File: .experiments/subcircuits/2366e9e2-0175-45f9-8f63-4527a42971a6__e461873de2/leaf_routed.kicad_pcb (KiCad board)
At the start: 2 copper layers, 49.9 x 20.9 mm, 7 parts, among them J2 Output, J3 Debug, U5 AP2112K-3.3

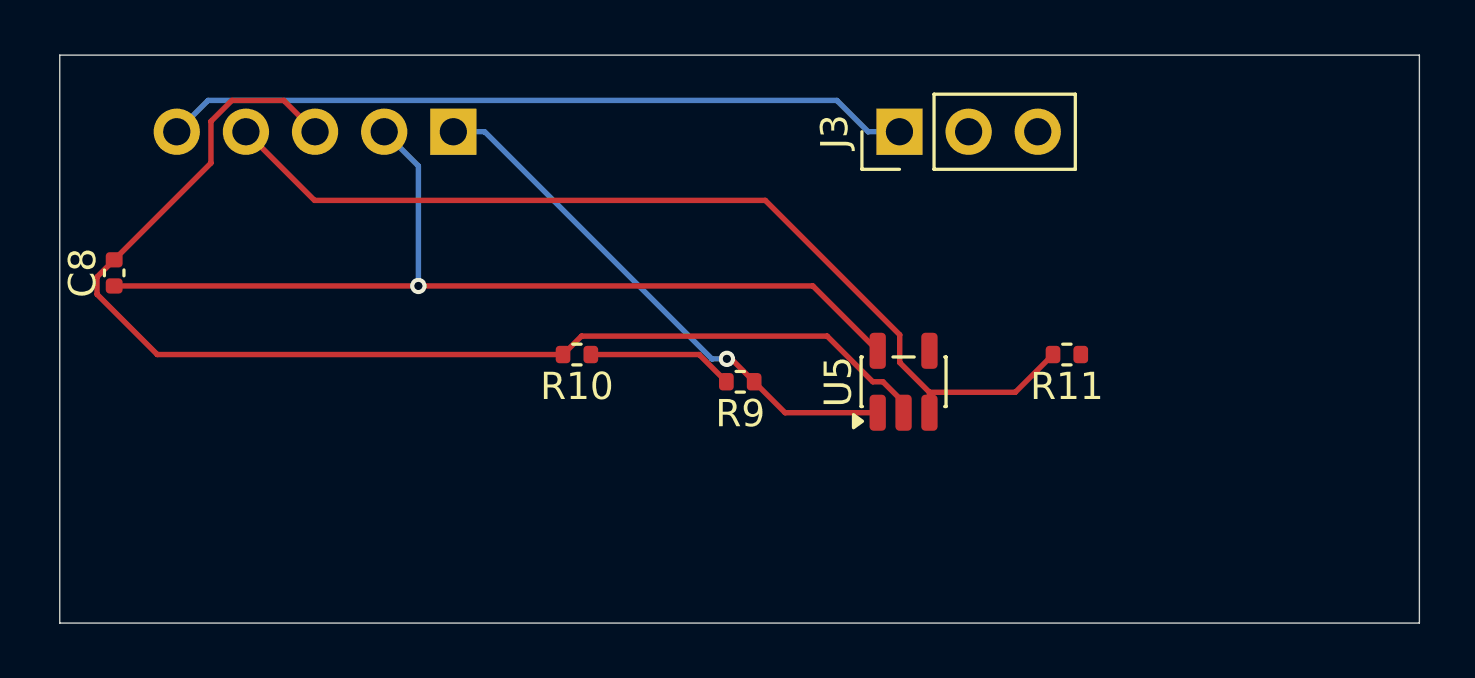
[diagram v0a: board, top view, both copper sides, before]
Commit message: feat: parent board stamping with preserved child copper
- Add --pcb, --stamp, --route, --jar flags to compose_subcircuits.py
- Implement subprocess-based parent board stamping (no pcbnew in main process)
- Add _stamp_parent_board() that copies base PCB, moves footprints to
  composed positions, clears existing tracks/zones, recreates child copper
  traces and vias with proper net name resolution
- Add _route_parent_board() for FreeRouting with preserve_existing_copper
- Add _persist_parent_artifact() for parent solved_layout.json persistence
- Store ParentComposition on ParentCompositionState for downstream access
- Update leaf artifacts from fresh pipeline run (6/6 leaves routed)
- Parent stamp verified: 37 components, 286 child traces, 10 vias preserved
  on real .kicad_pcb board with correct positions and net assignments
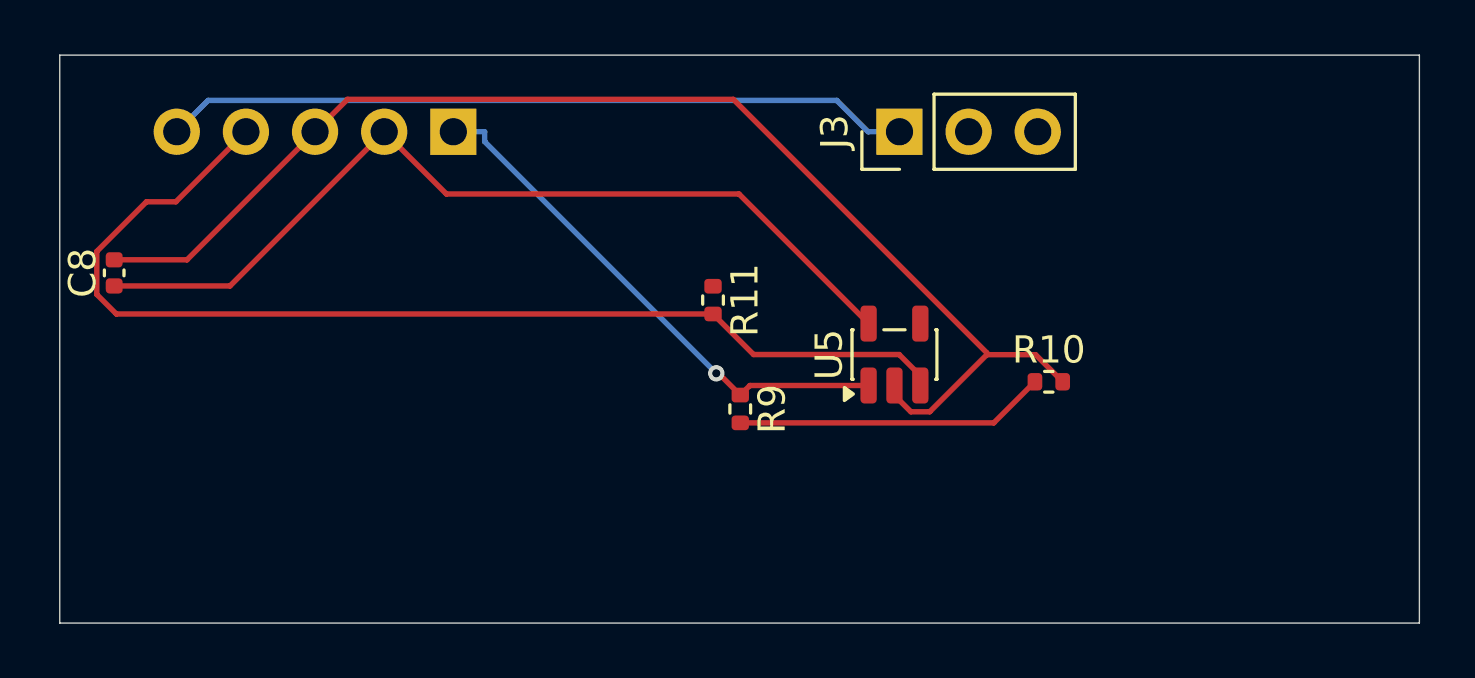
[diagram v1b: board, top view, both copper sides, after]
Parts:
- moved R10 17.4 mm to (36.3, 12.0), turned to 0 degrees
- moved R11 13.2 mm to (24.0, 9.00), turned to -90 degrees
- moved U5 1.05 mm to (30.7, 11.0)
- moved R9 1.00 mm to (25.0, 13.0), turned to -90 degrees
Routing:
- net Net-(U4-FB): track 5.39 -> 11.5 mm
- net /EN: track 35.5 -> 40.7 mm
- net /3V3: track 35.2 -> 33.0 mm, vias 1 -> 0
- net GND: track 44.9 -> 46.5 mm

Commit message: feat: unified hierarchical solver (solve_hierarchy.py)
Single-command entry point for the full subcircuit pipeline:
  python3 solve_hierarchy.py LLUPS.kicad_sch --pcb LLUPS.kicad_pcb --route

Phase 1: Solve leaf subcircuits (delegates to solve_subcircuits.py)
  - 6 leaves solved and routed via FreeRouting
  - Canonical copper persisted in solved_layout.json

Phase 2: Compose and route parent (delegates to compose_subcircuits.py)
  - Grid layout of 6 children with 5mm spacing
  - Child copper preserved on stamped parent board
  - FreeRouting routes interconnect nets between subcircuits
  - Parent artifact persisted with full copper

Flags: --skip-leaves, --leaf-only, --rounds, --mode, --spacing-mm, --jar
Full pipeline completes in ~4 minutes (with routing)
Skip-leaves mode completes in ~28 seconds
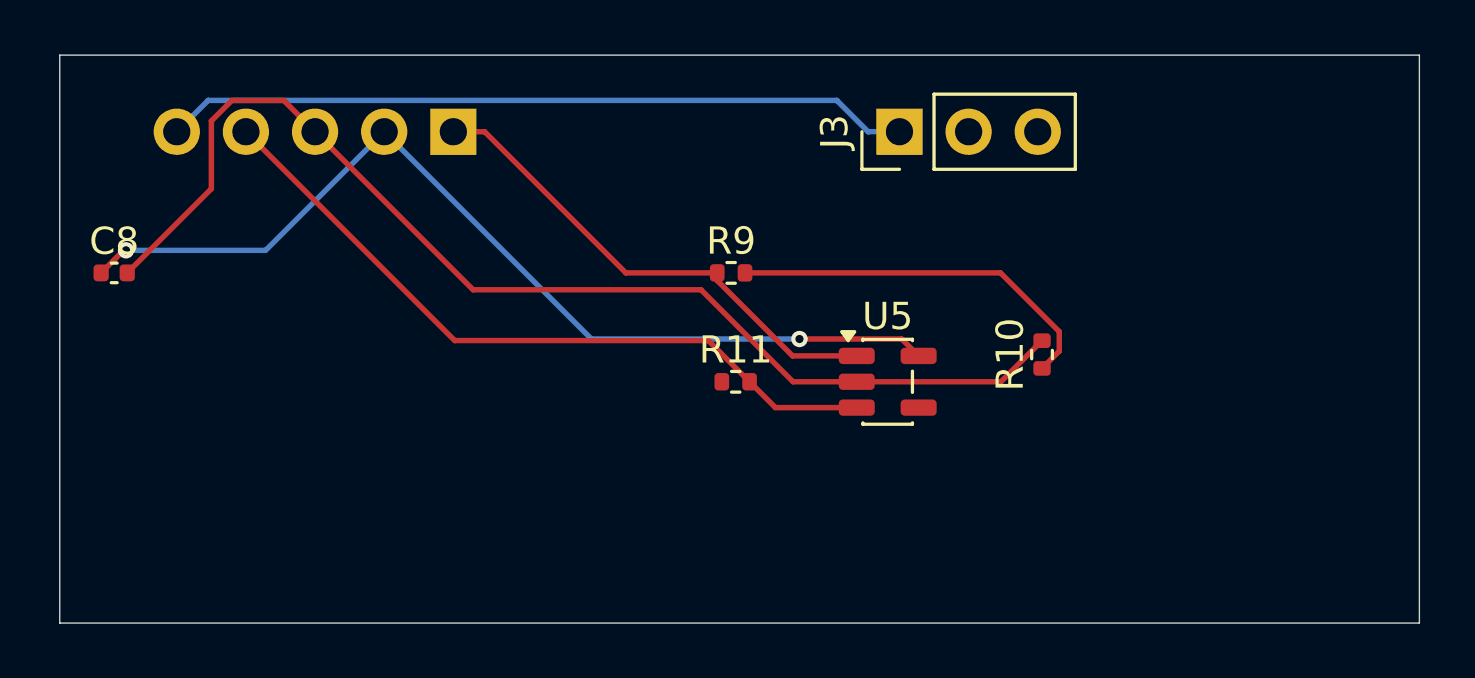
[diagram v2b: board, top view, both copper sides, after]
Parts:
- moved R9 5.01 mm to (24.7, 8.00), turned to 0 degrees
- moved R11 3.11 mm to (24.8, 12.0), turned to 0 degrees
- moved U5 1.03 mm to (30.4, 12.0), turned to 0 degrees
- moved R10 1.03 mm to (36.1, 11.0), turned to 90 degrees
- turned C8 to 0 degrees
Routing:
- net /EN: track 40.7 -> 26.6 mm
- net GND: track 46.5 -> 42.6 mm
- net /3V3: track 33.0 -> 35.6 mm, vias 0 -> 2
- net Net-(U4-FB): track 11.5 -> 14.1 mm
- net /5V: track 19.6 -> 18.4 mm, vias 1 -> 0
